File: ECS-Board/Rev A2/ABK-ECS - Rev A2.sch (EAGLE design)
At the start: 169 parts, among them J1 22-27-2061-06, J2 USB-B-S-RA, J3 1241050-5, J4 MSTBA2, J5 22-05-7068-06, J6 22-05-7028-02, J7 22-05-7068-06, J8 22-05-7028-02, K1 G6K-2G-Y, SW1 B3FS-1015, SW2 B3FS-1015, T1 EXMACHINA-LOGO-NAME, T10 MMBT2222AL, T11 IRLML5103TRPBF, T2 IRLML5103TRPBF, T3 MMBT2222AL, T4 MMBT2222AL, T5 IRLML5103TRPBF, T6 MMBT2222AL, T7 IRLML5103TRPBF, T8 MMBT2222AL, T9 IRLML5103TRPBF, U1 AT24C512C-SSHM-B, U2 LPC1768FBD100, U3 LT3686HDDPBF, U4 LT3686HDDPBF, U5 CD4050BD, X1 FC-135, X2 ASE-12, X3 3000

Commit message: Add rev A2 and modify board
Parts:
- added R75: 1K5, rcl:R-EU_R0603
- F1: value FUSE3557L -> 1812L110/24DR; device fuse2:FUSE3557L -> fuse2:1812L110/24DR
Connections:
- net MOTOR_CTR renamed R_VALIDATION
- removed net 230V-DETECTION: C20.1, R38.2, U2.P1[27]/CLKOUT/*USB_OVRCR/CAP0[1]
- net +3V3: now also R75.1, U2.VDDA
- net 230V_DETECTION: now also C20.1, R38.2
- net N$2: now also R75.2
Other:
- moved on the sheet: R4, R5

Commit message: Add input and output to the board and LDO 5V to 3.3V for FTDI connector
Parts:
- added C22, C23, C24: 0.1uF, rcl:C-EUC0603
- added C25, C26: 1u, rcl:C-EUC0603
- added D10, D11, D12, D13: 1N4148WS, diode:1N4148WS
- added J10: 22-05-7068-06, con-molex:22-05-7068-06
- added J9: 22-05-7028-02, con-molex:22-05-7028-02
- added LED17, LED18, LED19, LED20, LED21, LED22, LED23: Blue, led:LEDCHIPLED_0603
- added OK3, OK4: TLP283-4, optocoupler:TLP283-4
- added R100, R101, R102, R103: 1K5, rcl:R-EU_R0603
- added R104, R105, R106, R107, R76, R77, R78, R79: 4K7, rcl:R-EU_R0603
- added R108, R109, R110, R111, R80, R81, R82, R83: 1K, rcl:R-EU_R0603
- added R112, R113, R114, R115, R84, R85, R86, R87, R92, R93, R94, R95: 330, rcl:R-EU_R0603
- added R88, R89, R90, R91: 10K, rcl:R-EU_R0603
- added R96, R97, R98, R99: 100, rcl:R-EU_R0603
- added T12, T13, T14, T15: IRLML5103TRPBF, International_Rectifier_By_element14_Batch_1:IRLML5103TRPBF
- added T16, T17, T18, T19: MMBT2222AL, transistor:MMBT2222AL
- added U6, U7, U8: SN74LVC2G17DBVR, ti:SN74LVC2G17DBVR
- added U9: TC1264-3.3, microchip-6:TC1264-3.3
- J7: value 22-05-7068-06 -> 22-05-7058-05; device con-molex:22-05-7068-06 -> con-molex:22-05-7058-05; MPN 22-05-7068 -> (none); OC_NEWARK 89K0316 -> (none)
- J8: value 22-05-7028-02 -> 22-05-7068-06; device con-molex:22-05-7028-02 -> con-molex:22-05-7068-06; MPN 22-05-7028 -> 22-05-7068; OC_NEWARK 25M1728 -> 89K0316
- OK2: MF VISHAY/TELEFUNKEN -> (none); MPN TCMT4100 -> (none); OC_NEWARK 06H1639 -> (none)
- R10: value 10K -> 0R; MPN MCMR06X1002FTL -> MCMR06X000 PTL; OC_NEWARK 86T3506 -> 86T3500
- R11, R21: value 1K5 -> 10K; MPN MCMR06X1501FTL -> MCMR06X1002FTL; OC_NEWARK 86T3542 -> 86T3506
- R13: value 31K6 -> 1K5; MPN MCMR06X3162FTL -> MCMR06X1501FTL; OC_FARNELL 2073391 -> (none); OC_NEWARK 86T3613 -> 86T3542
- R15: value 4K7 -> 31K6; MPN MCMR06X4701FTL -> MCMR06X3162FTL; OC_FARNELL (none) -> 2073391; OC_NEWARK 86T3649 -> 86T3613
- R17: value 52K3 -> 4K7; MPN MC0063W0603152K3 -> MCMR06X4701FTL; OC_FARNELL 2073391 -> (none); OC_NEWARK 26M0962 -> 86T3649
- R18: value 10K -> 52K3; MPN MCMR06X1002FTL -> MC0063W0603152K3; OC_NEWARK 86T3506 -> 26M0962
- R19: value 31K6 -> 10K; MPN MCMR06X3162FTL -> MCMR06X1002FTL; OC_NEWARK 86T3613 -> 86T3506
- R20: value 10K -> 31K6; MPN MCMR06X1002FTL -> MCMR06X3162FTL; OC_NEWARK 86T3506 -> 86T3613
- R23: value 100 -> 1K5; MPN MCMR06X1000FTL -> MCMR06X1501FTL; OC_FARNELL (none) -> 2073391; OC_NEWARK 86T3504 -> 86T3542
- R24, R68, R69, R70: value 1K -> 100; MPN MCMR06X1001FTL -> MCMR06X1000FTL; OC_NEWARK 86T3505 -> 86T3504
- R32: value 4K7 -> 1K; MPN MCMR06X4701FTL -> MCMR06X1001FTL; OC_NEWARK 86T3649 -> 86T3505
- R37: value 1K5 -> 4K7; MPN MCMR06X1501FTL -> MCMR06X4701FTL; OC_NEWARK 86T3542 -> 86T3649
- R40, R41, R42, R43: value 1K5 -> 1K; MPN MCMR06X1501FTL -> MCMR06X1001FTL; OC_NEWARK 86T3542 -> 86T3505
- R44: value 330 -> 1K; MPN MCMR06X4701FTL -> MCMR06X1001FTL; OC_NEWARK 86T3649 -> 86T3505
- R45: value 10K -> 1K; MPN MCMR06X4701FTL -> MCMR06X1001FTL; OC_NEWARK 86T3649 -> 86T3505
- R46: value 100 -> 4K7; MPN MCMR06X1000FTL -> MCMR06X4701FTL; OC_NEWARK 86T3504 -> 86T3649
- R47: value 330 -> 4K7
- R48: value 10K -> 4K7
- R49, R51, R53: value 330 -> 1K5; MPN MCMR06X4701FTL -> MCMR06X1501FTL; OC_NEWARK 86T3649 -> 86T3542
- R50, R52, R54: value 10K -> 1K5; MPN MCMR06X4701FTL -> MCMR06X1501FTL; OC_NEWARK 86T3649 -> 86T3542
- R55, R56: value 100 -> 1K5; MPN MCMR06X1000FTL -> MCMR06X1501FTL; OC_NEWARK 86T3504 -> 86T3542
- R57: value 100 -> 10K; MPN MCMR06X1000FTL -> MCMR06X4701FTL; OC_NEWARK 86T3504 -> 86T3649
- R58: value 100 -> 330; MPN MCMR06X1000FTL -> MCMR06X4701FTL; OC_NEWARK 86T3504 -> 86T3649
- R59: value 1K5 -> 100; MPN MCMR06X1501FTL -> MCMR06X1000FTL; OC_NEWARK 86T3542 -> 86T3504
- R60, R61, R62: value 1K5 -> 10K; MPN MCMR06X1501FTL -> MCMR06X4701FTL; OC_NEWARK 86T3542 -> 86T3649
- R63: value 4K7 -> 10K
- R64, R65, R66: value 4K7 -> 330
- R67: value 1K -> 330; MPN MCMR06X1001FTL -> MCMR06X4701FTL; OC_NEWARK 86T3505 -> 86T3649
- R7: value 10K -> 1K5; MPN MCMR06X1002FTL -> MCMR06X1501FTL; OC_NEWARK 86T3506 -> 86T3542
- R71: value 330 -> 100; MPN MCMR06X3300FTL -> MCMR06X1000FTL; OC_NEWARK 86T3616 -> 86T3504
- R72, R73, R74: value 330 -> 1K5; MPN MCMR06X3300FTL -> MCMR06X1501FTL; OC_NEWARK 86T3616 -> 86T3542
- R8: value 0R -> 10K; MPN MCMR06X000 PTL -> MCMR06X1002FTL; OC_NEWARK 86T3500 -> 86T3506
- T11, T9: value IRLML5103TRPBF -> MMBT2222AL; device International_Rectifier_By_element14_Batch_1:IRLML5103TRPBF -> transistor:MMBT2222AL
- T4, T6: value MMBT2222AL -> IRLML5103TRPBF; device transistor:MMBT2222AL -> International_Rectifier_By_element14_Batch_1:IRLML5103TRPBF
- U5: value CD4050BD -> SN74LVC2G17DBVR; device TI-CD4050BD:CD4050BD -> ti:SN74LVC2G17DBVR
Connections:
- new net INPUT: LED15.A, R45.2, R48.1, U8.2A
- new net INPUT_MCU: U2.P0[16]/RXD1/SSEL0/SSEL, U8.2Y
- new net LED1: D10.1, J10-2.S, R88.2, T12.D
- new net LED1_MCU: R112.2, U2.P0[0]/RD1/TXD3/SDA1
- new net LED2: D11.1, J10-3.S, R89.2, T13.D
- new net LED2_MCU: R113.2, U2.P1[29]/MCOB2/PCAP1[1]/MAT0[1]
- new net LED3: D12.1, J10-4.S, R90.2, T14.D
- new net LED3_MCU: R114.2, U2.P1[28]/MCOA2/PCAP1[0]/MAT0[0]
- new net LED4: D13.1, J10-5.S, R91.2, T15.D
- new net LED4_MCU: R115.2, U2.P1[27]/CLKOUT/*USB_OVRCR/CAP0[1]
- new net N$100: OK2A.EMIT, R43.1
- new net N$101: OK2B.A, R41.2
- new net N$102: J7-3.S, R41.1
- new net N$103: OK2B.EMIT, R44.1
- new net N$104: OK2C.A, R42.2
- new net N$105: J7-2.S, R42.1
- new net N$106: OK2C.EMIT, R45.1
- new net N$107: LED13.C, R54.1
- new net N$108: LED14.C, R55.1
- new net N$109: LED15.C, R56.1
- new net N$31: LED20.A, R104.1, R108.1, R96.1
- new net N$33: OK4A.EMIT, R108.2
- new net N$34: LED21.A, R105.1, R109.1, R97.1
- new net N$35: OK4B.EMIT, R109.2
- new net N$36: LED22.A, R106.1, R110.1, R98.1
- new net N$37: LED23.A, R107.1, R111.1, R99.1
- new net N$38: OK4C.EMIT, R110.2
- new net N$39: OK4D.EMIT, R111.2
- new net N$40: OK4A.A, R112.1
- new net N$42: OK4B.A, R113.1
- new net N$43: OK4D.A, R115.1
- new net N$46: OK4C.A, R114.1
- new net N$66: LED20.C, R100.1
- new net N$67: LED21.C, R101.1
- new net N$68: LED22.C, R102.1
- new net N$69: LED23.C, R103.1
- new net N$71: R92.1, T12.G, T16.C
- new net N$72: R93.1, T13.G, T17.C
- new net N$77: R94.1, T14.G, T18.C
- new net N$78: R95.1, T15.G, T19.C
- new net N$81: OK2A.A, R40.2
- new net N$82: J7-4.S, R40.1
- new net N$84: R96.2, T16.B
- new net N$85: R97.2, T17.B
- new net N$98: R98.2, T18.B
- new net N$99: R99.2, T19.B
- new net SLOWFEED_1: LED13.A, R43.2, R46.1, U7.1A
- new net SLOWFEED_1_MCU: U2.P0[15]/TXD1/SCK0/SCK, U7.1Y
- new net SLOWFEED_2: LED14.A, R44.2, R47.1, U7.2A
- new net SLOWFEED_2_MCU: U2.P0[17]/CTS1/MISO0/MISO, U7.2Y
- net !RESET: now also R11.1; no longer R10.1
- net +24V: now also J10-1.S, J8-1.S, R17.2, R58.2, R64.2, R65.2, R66.2, R67.2, R92.2, R93.2, R94.2, R95.2, T12.S, T13.S, T14.S, T15.S, T4.S, T6.S; no longer R15.2, R44.2, R47.2, R49.2, R51.2, R53.2, T11.S, T9.S
- net +3V3: now also C22.1, C23.1, C24.1, C26.1, R11.2, R20.2, R23.2, R7.1, R8.2, U6.VCC, U7.VCC, U8.VCC, U9.VOUT; no longer R10.2, R19.2, R22.2, R7.2, R75.1
- net +5V: now also C25.1, J1-6.S, OK3A.COL, OK3B.COL, OK3C.COL, OK3D.COL, OK4A.COL, OK4B.COL, OK4C.COL, OK4D.COL, R18.2, R22.2, R37.1, U9.VIN; no longer OK2D.COL, R17.2, R21.2, R36.1
- net 230V_DETECTION: now also U8.1A; no longer U5.E
- net 230V_DETECTION_MCU: now also U8.1Y; no longer U5.K=E
- net BOOT_SELECT_P2_10: now also R9.1; no longer R8.1
- net BOOT_SELECT_P2_12: now also R10.1; no longer R9.1
- net BRAKE_CONTROL: now also D9.1, J8-5.S, R63.2, T7.D; no longer D8.1, J7-5.S, R54.2, T9.D
- net BRAKE_CONTROL_MCU: now also R87.2; no longer R74.2
- net CLUTCH_CONTROL: now also D8.1, J8-4.S, R62.2, T6.D; no longer D7.1, J7-4.S, R52.2, T7.D
- net CLUTCH_CONTROL_MCU: now also R86.2; no longer R73.2
- net DRIVE_STATUS_1: now also R31.2, R35.1, U6.1A; no longer R30.2, R34.1, U5.C
- net DRIVE_STATUS_1_MCU: now also U6.1Y; no longer U5.I=C
- net DRIVE_STATUS_2: now also R32.2, R36.1, U6.2A; no longer R31.2, R35.1, U5.D
- net DRIVE_STATUS_2_MCU: now also U6.2Y; no longer U5.J=D
- net EMERGENCY_STOP: now also R29.2, R33.1, U5.1A; no longer R28.2, R32.1, U5.A
- net EMERGENCY_STOP_MCU: now also U5.1Y; no longer U5.G=A
- net GND: now also C22.2, C23.2, C24.2, C25.2, C26.2, D10.2, D11.2, D12.2, D13.2, J10-6.S, J7-5.S, J8-6.S, J9-2.S, OK3A.C, OK3B.C, OK3C.C, OK3D.C, OK4A.C, OK4B.C, OK4C.C, OK4D.C, R100.2, R101.2, R102.2, R103.2, R104.2, R105.2, R106.2, R107.2, R13.2, R15.1, R19.1, R21.1, R36.2, R46.2, R47.2, R48.2, R49.2, R50.2, R51.2, R52.2, R53.2, R54.2, R55.2, R56.2, R57.1, R60.1, R61.1, R62.1, R63.1, R72.2, R73.2, R74.2, R75.2, R76.2, R77.2, R78.2, R79.2, R88.1, R89.1, R90.1, R91.1, T11.E, T16.E, T17.E, T18.E, T19.E, T9.E, U5.GND, U6.GND, U7.GND, U8.GND, U9.GND, U9.GND_2; no longer J7-6.S, J8-2.S, OK2D.C, R11.2, R13.1, R18.1, R20.1, R32.2, R37.2, R40.2, R41.2, R42.2, R43.2, R45.1, R48.1, R50.1, R52.1, R54.1, R59.2, R60.2, R61.2, R62.2, R63.2, R64.2, R65.2, R66.2, T4.E, T6.E, U5.VSS
- net LIMIT_SWITCH: now also R30.2, R34.1, U5.2A; no longer R29.2, R33.1, U5.B
- net LIMIT_SWITCH_MCU: now also U5.2Y; no longer U5.H=B
- net L_VALIDATION: now also D7.1, J8-3.S, R61.2; no longer D6.1, J7-3.S, R48.2
- net L_VALIDATION_MCU: now also R85.2; no longer R72.2
- net MOTOR_CONTROL_MCU: now also R59.2; no longer R46.2
- net N$1: now also R7.2; no longer R6.2
- net N$13: now also R20.1, R21.2; no longer R19.1, R20.2
- net N$17: now also R68.2, T8.B; no longer R55.2, T3.B
- net N$18: now also R64.1, T4.G, T8.C; no longer R51.1, T2.G, T3.C
- net N$19: now also R69.2, T9.B; no longer R56.2, T4.B
- net N$2: now also R6.2; no longer R75.2
- net N$20: now also R65.1, T9.C; no longer R47.1, T4.C
- net N$21: now also R70.2, T10.B; no longer R57.2, T6.B
- net N$22: now also R66.1, T10.C, T6.G; no longer R49.1, T6.C, T7.G
- net N$23: now also R71.2, T11.B; no longer R58.2, T8.B
- net N$24: now also R67.1, T11.C, T7.G; no longer R53.1, T8.C, T9.G
- net N$25: now also R59.1, T3.B; no longer R46.1, T10.B
- net N$26: now also R58.1, T2.G, T3.C; no longer R44.1, T10.C, T11.G
- net N$28: now also R24.2; no longer R23.2
- net N$29: now also R12.1; no longer R11.1
- net N$3: now also R13.1; no longer R12.1
- net N$30: now also D5.1, J9-1.S, R57.2, T2.D; no longer D9.1, J8-1.S, R45.2, T11.D
- net N$32: now also R24.1; no longer R23.1
- net N$4: now also R14.2; no longer R13.2
- net N$41: now also R25.2; no longer R24.2
- net N$44: now also R17.1; no longer R16.1
- net N$45: now also R16.1; no longer R15.1
- net N$47: now also R26.2; no longer R25.2
- net N$48: now also R27.2; no longer R26.2
- net N$49: now also R28.2; no longer R27.2
- net N$5: now also R10.2, R8.1; no longer R7.1, R8.2
- net N$50: now also R23.1; no longer R22.1
- net N$51: now also R22.1; no longer R21.1
- net N$52: now also R28.1; no longer R27.1
- net N$53: now also R27.1; no longer R26.1
- net N$54: now also R26.1; no longer R25.1
- net N$55: now also R25.1; no longer R24.1
- net N$56: now also R49.1; no longer R37.1
- net N$57: now also R50.1; no longer R40.1
- net N$58: now also R51.1; no longer R41.1
- net N$59: now also R52.1; no longer R42.1
- net N$61: now also R32.1; no longer R31.1
- net N$62: now also R31.1; no longer R30.1
- net N$63: now also R30.1; no longer R29.1
- net N$64: now also R29.1; no longer R28.1
- net N$65: now also R53.1; no longer R43.1
- net N$7: now also R15.2; no longer R14.2
- net N$73: now also R37.2; no longer R36.2
- net N$75: now also LED16.A, R68.1, R76.1, R80.1; no longer LED13.A, R55.1, R63.1, R67.1
- net N$76: now also OK3A.EMIT, R80.2; no longer OK2A.EMIT, R67.2
- net N$79: now also LED17.A, R69.1, R77.1, R81.1; no longer LED14.A, R56.1, R64.1, R68.1
- net N$80: now also OK3B.EMIT, R81.2; no longer OK2B.EMIT, R68.2
- net N$83: now also LED18.A, R70.1, R78.1, R82.1; no longer LED15.A, R57.1, R65.1, R69.1
- net N$86: now also LED19.A, R71.1, R79.1, R83.1; no longer LED16.A, R58.1, R66.1, R70.1
- net N$87: now also OK3C.EMIT, R82.2; no longer OK2C.EMIT, R69.2
- net N$88: now also OK3D.EMIT, R83.2; no longer OK2D.EMIT, R70.2
- net N$89: now also OK3A.A, R84.1; no longer OK2A.A, R71.1
- net N$9: now also R18.1, R19.2; no longer R17.1, R18.2
- net N$91: now also OK3B.A, R85.1; no longer OK2B.A, R72.1
- net N$92: now also OK3D.A, R87.1; no longer OK2D.A, R74.1
- net N$93: now also OK3C.A, R86.1; no longer OK2C.A, R73.1
- net N$94: now also LED16.C, R72.1; no longer LED13.C, R59.1
- net N$95: now also LED17.C, R73.1; no longer LED14.C, R60.1
- net N$96: now also LED18.C, R74.1; no longer LED15.C, R61.1
- net N$97: now also LED19.C, R75.1; no longer LED16.C, R62.1
- net R_VALIDATION: now also D6.1, J8-2.S, R60.2, T4.D; no longer D5.1, J7-2.S, R50.2, T2.D
- net R_VALIDATION_MCU: now also R84.2; no longer R71.2

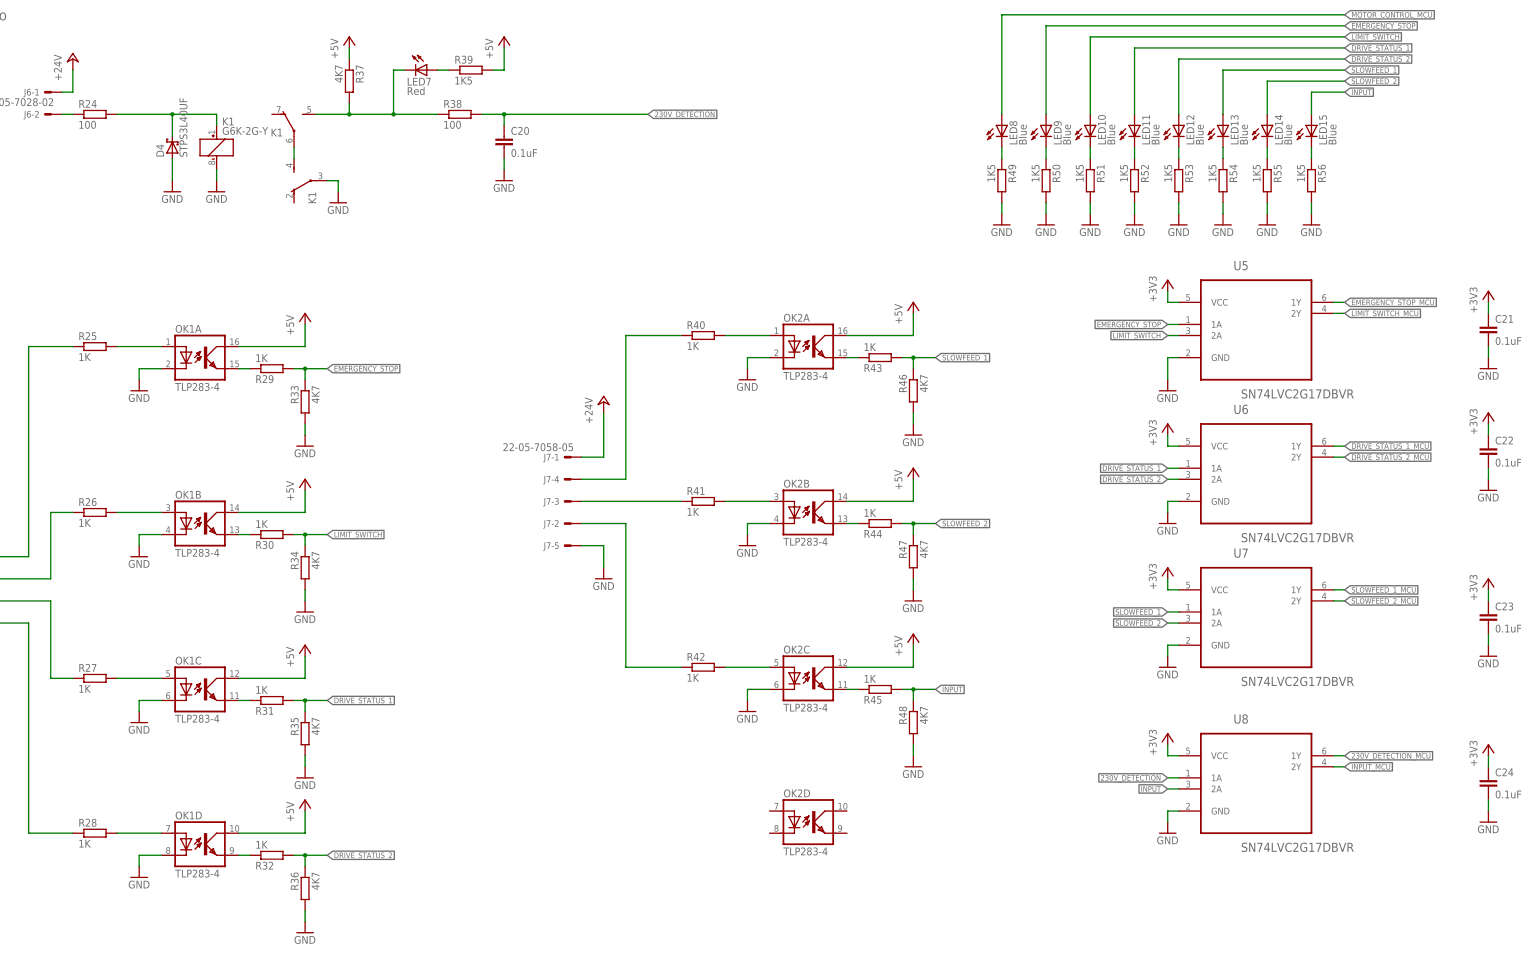
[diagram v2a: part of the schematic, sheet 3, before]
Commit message: Add pullup resistor on AT24C WP Separate +5V from ISP connector and the +5V general and add a diode Change +5V--->+3V3 conversion methode on input Wired OK2D
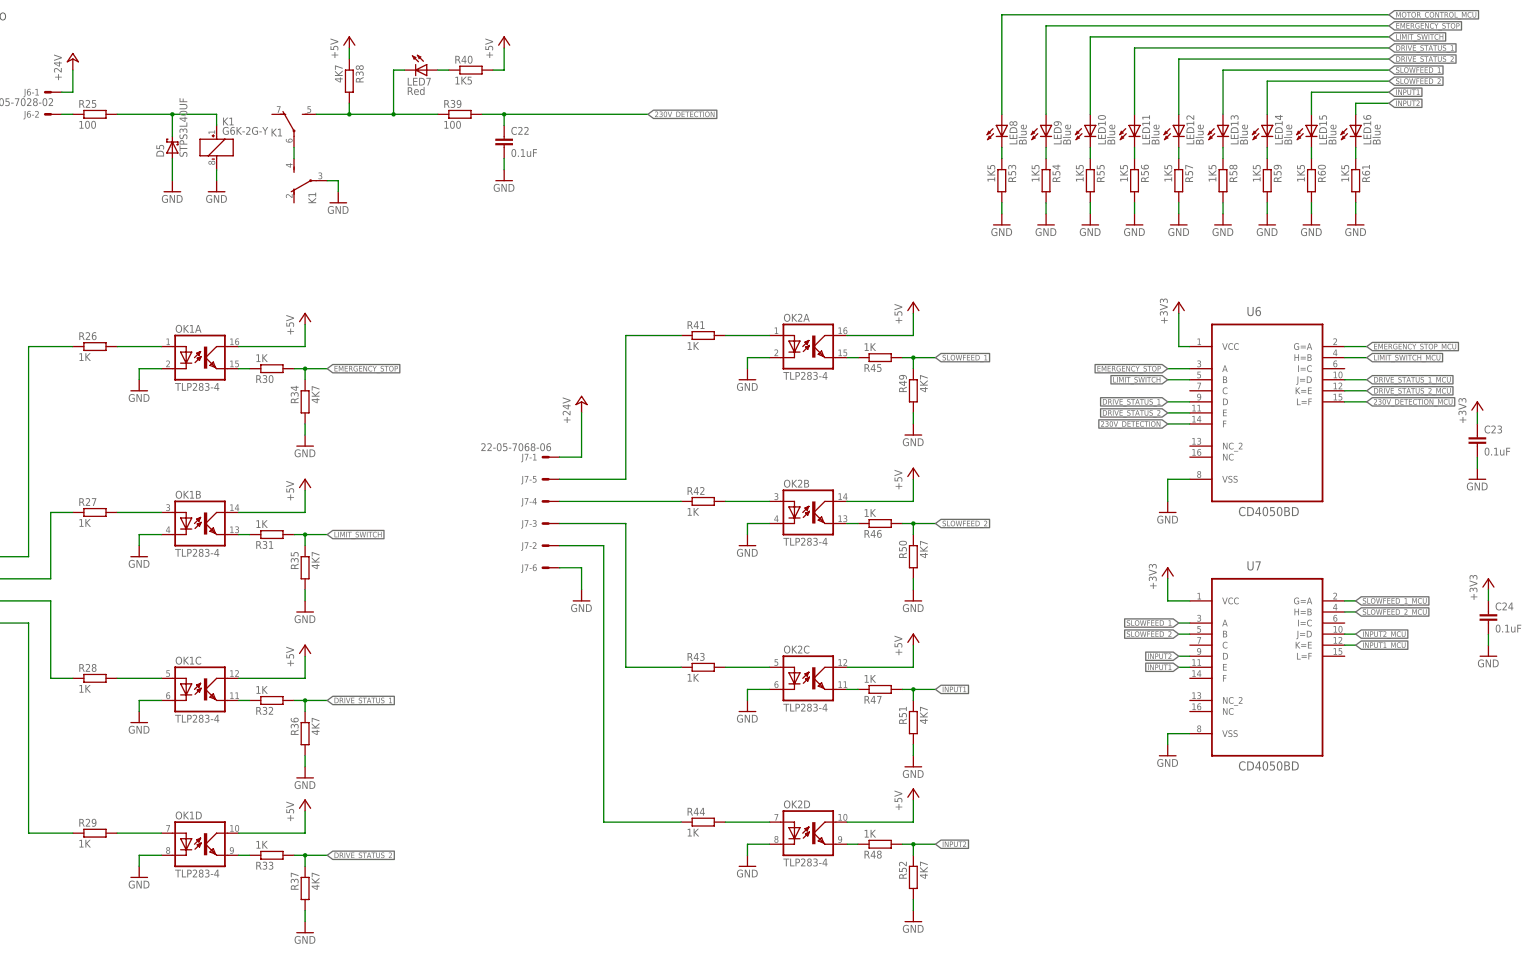
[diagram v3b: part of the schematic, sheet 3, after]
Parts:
- removed C25, C26: 1u, rcl:C-EUC0603
- removed U8: SN74LVC2G17DBVR, ti:SN74LVC2G17DBVR
- removed U9: TC1264-3.3, microchip-6:TC1264-3.3
- added D14: 1N4148WS, diode:1N4148WS
- added LED24: Blue, led:LEDCHIPLED_0603
- added R116: 1K, rcl:R-EU_R0603
- added R117, R118, R119, R120: 330, rcl:R-EU_R0603
- C20, C21: value 0.1uF -> 1u; MPN MC0603B104K160CT -> (none); OC_NEWARK 06R4923 -> (none)
- D5: value 1N4148WS -> STPS3L40UF; device diode:1N4148WS -> diode:STPS3L40UF; OC_NEWARK (none) -> 06X0873
- J7: value 22-05-7058-05 -> 22-05-7068-06; device con-molex:22-05-7058-05 -> con-molex:22-05-7068-06
- R100, R72: value 1K5 -> 330; MPN MCMR06X1501FTL -> MCMR06X4701FTL; OC_NEWARK 86T3542 -> 86T3649
- R101, R102, R103, R39, R73, R74, R75: value 1K5 -> 100; MPN MCMR06X1501FTL -> MCMR06X1000FTL; OC_NEWARK 86T3542 -> 86T3504
- R104, R76: value 4K7 -> 100; MPN MCMR06X4701FTL -> MCMR06X1000FTL; OC_NEWARK 86T3649 -> 86T3504
- R105, R106, R107, R77, R78, R79: value 4K7 -> 1K5; MPN MCMR06X4701FTL -> MCMR06X1501FTL; OC_NEWARK 86T3649 -> 86T3542
- R108, R40, R80: value 1K -> 1K5; MPN MCMR06X1001FTL -> MCMR06X1501FTL; OC_NEWARK 86T3505 -> 86T3542
- R109, R110, R111, R81, R82, R83: value 1K -> 4K7; MPN MCMR06X1001FTL -> MCMR06X4701FTL; OC_NEWARK 86T3505 -> 86T3649
- R11: value 10K -> 0R; MPN MCMR06X1002FTL -> MCMR06X000 PTL; OC_NEWARK 86T3506 -> 86T3500
- R112, R84: value 330 -> 4K7; MPN MCMR06X3300FTL -> MCMR06X4701FTL; OC_NEWARK 86T3616 -> 86T3649
- R113, R114, R115, R85, R86, R87: value 330 -> 1K; MPN MCMR06X3300FTL -> MCMR06X1001FTL; OC_NEWARK 86T3616 -> 86T3505
- R12, R22: value 1K5 -> 10K; MPN MCMR06X1501FTL -> MCMR06X1002FTL; OC_NEWARK 86T3542 -> 86T3506
- R14: value 31K6 -> 1K5; MPN MCMR06X3162FTL -> MCMR06X1501FTL; OC_FARNELL 2073391 -> (none); OC_NEWARK 86T3613 -> 86T3542
- R16: value 4K7 -> 31K6; MPN MCMR06X4701FTL -> MCMR06X3162FTL; OC_FARNELL (none) -> 2073391; OC_NEWARK 86T3649 -> 86T3613
- R18: value 52K3 -> 4K7; MPN MC0063W0603152K3 -> MCMR06X4701FTL; OC_FARNELL 2073391 -> (none); OC_NEWARK 26M0962 -> 86T3649
- R19: value 10K -> 52K3; MPN MCMR06X1002FTL -> MC0063W0603152K3; OC_NEWARK 86T3506 -> 26M0962
- R20: value 31K6 -> 10K; MPN MCMR06X3162FTL -> MCMR06X1002FTL; OC_NEWARK 86T3613 -> 86T3506
- R21: value 10K -> 31K6; MPN MCMR06X1002FTL -> MCMR06X3162FTL; OC_NEWARK 86T3506 -> 86T3613
- R24: value 100 -> 1K5; MPN MCMR06X1000FTL -> MCMR06X1501FTL; OC_FARNELL (none) -> 2073391; OC_NEWARK 86T3504 -> 86T3542
- R25: value 1K -> 100; MPN MCMR06X1001FTL -> MCMR06X1000FTL; OC_NEWARK 86T3505 -> 86T3504
- R33, R46, R47, R48: value 4K7 -> 1K; MPN MCMR06X4701FTL -> MCMR06X1001FTL; OC_NEWARK 86T3649 -> 86T3505
- R38: value 100 -> 4K7; MPN MCMR06X1000FTL -> MCMR06X4701FTL; OC_NEWARK 86T3504 -> 86T3649
- R4: value 33 -> 4K7; MPN MCMR06X33R0FTL -> MCMR06X4701FTL; OC_NEWARK 86T3614 -> 86T3649
- R49, R50, R51, R52: value 1K5 -> 4K7; MPN MCMR06X1501FTL -> MCMR06X4701FTL; OC_NEWARK 86T3542 -> 86T3649
- R57, R60, R61: value 10K -> 1K5; MPN MCMR06X4701FTL -> MCMR06X1501FTL; OC_NEWARK 86T3649 -> 86T3542
- R58: value 330 -> 1K5; MPN MCMR06X4701FTL -> MCMR06X1501FTL; OC_NEWARK 86T3649 -> 86T3542
- R59: value 100 -> 1K5; MPN MCMR06X1000FTL -> MCMR06X1501FTL; OC_NEWARK 86T3504 -> 86T3542
- R6: value 1K5 -> 33; MPN MCMR06X1501FTL -> MCMR06X33R0FTL; OC_NEWARK 86T3542 -> 86T3614
- R63: value 10K -> 330
- R64: value 330 -> 100; MPN MCMR06X4701FTL -> MCMR06X1000FTL; OC_NEWARK 86T3649 -> 86T3504
- R65, R66, R67, R93, R94, R95: value 330 -> 10K
- R68, R96: value 100 -> 10K; MPN MCMR06X1000FTL -> MCMR06X4701FTL; OC_NEWARK 86T3504 -> 86T3649
- R69, R70, R71, R97, R98, R99: value 100 -> 330; MPN MCMR06X1000FTL -> MCMR06X4701FTL; OC_NEWARK 86T3504 -> 86T3649
- R8: value 10K -> 1K5; MPN MCMR06X1002FTL -> MCMR06X1501FTL; OC_NEWARK 86T3506 -> 86T3542
- R88: value 10K -> 1K; MPN MCMR06X4701FTL -> MCMR06X1001FTL; OC_NEWARK 86T3649 -> 86T3505
- R89, R90, R91: value 10K -> 330; MPN MCMR06X4701FTL -> MCMR06X3300FTL; OC_NEWARK 86T3649 -> 86T3616
- R9: value 0R -> 10K; MPN MCMR06X000 PTL -> MCMR06X1002FTL; OC_NEWARK 86T3500 -> 86T3506
- R92: MPN MCMR06X4701FTL -> MCMR06X3300FTL; OC_NEWARK 86T3649 -> 86T3616
- U5: value SN74LVC2G17DBVR -> TC1264-3.3; device ti:SN74LVC2G17DBVR -> microchip-6:TC1264-3.3
- U6, U7: value SN74LVC2G17DBVR -> CD4050BD; device ti:SN74LVC2G17DBVR -> ti:CD4050BD
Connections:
- removed net INPUT: LED15.A, R45.2, R48.1, U8.2A
- removed net INPUT_MCU: U2.P0[16]/RXD1/SSEL0/SSEL, U8.2Y
- new net +5V/1: C20.1, D4.C, J1-6.S, U5.VIN
- new net INPUT1: LED15.A, R47.2, R51.1, U7.E
- new net INPUT1_MCU: U2.P0[16]/RXD1/SSEL0/SSEL, U7.K=E
- new net INPUT2: LED16.A, R48.2, R52.1, U7.D
- new net INPUT2_MCU: U2.P2[9]/USB_CONNECT/RXD2, U7.J=D
- new net N$110: OK2D.EMIT, R48.1
- new net N$111: OK2D.A, R44.2
- new net N$112: J7-2.S, R44.1
- new net N$90: LED16.C, R61.1
- net !RESET: now also R12.1; no longer R11.1
- net +24V: now also R100.2, R18.2, R63.2, R69.2, R70.2, R71.2, R72.2, R97.2, R98.2, R99.2; no longer R16.2, R58.2, R64.2, R65.2, R66.2, R67.2, R92.2, R93.2, R94.2, R95.2
- net +3V3: now also R1.1, R12.2, R21.2, R24.2, R4.2, R8.1, R9.2, U5.VOUT; no longer C22.1, C26.1, R11.2, R2.2, R20.2, R23.2, R6.1, R8.2, U5.VCC, U8.VCC, U9.VOUT
- net +5V: now also OK2D.COL, R19.2, R23.2, R38.1, R40.2; no longer C25.1, J1-6.S, R18.2, R22.2, R37.1, R39.2, U9.VIN
- net 230V_DETECTION: now also C22.1, R39.2, U6.F; no longer C20.1, R38.2, U8.1A
- net 230V_DETECTION_MCU: now also U6.L=F; no longer U8.1Y
- net BOOT_SELECT_P2_10: now also R10.1; no longer R9.1
- net BOOT_SELECT_P2_12: now also R11.1; no longer R10.1
- net BRAKE_CONTROL: now also D10.1, R68.2; no longer D9.1, R63.2
- net BRAKE_CONTROL_MCU: now also R92.2; no longer R87.2
- net CLUTCH_CONTROL: now also D9.1, R67.2; no longer D8.1, R62.2
- net CLUTCH_CONTROL_MCU: now also R91.2; no longer R86.2
- net DRIVE_STATUS_1: now also R32.2, R36.1, U6.D; no longer R31.2, R35.1, U6.1A
- net DRIVE_STATUS_1_MCU: now also U6.J=D; no longer U6.1Y
- net DRIVE_STATUS_2: now also R33.2, R37.1, U6.E; no longer R32.2, R36.1, U6.2A
- net DRIVE_STATUS_2_MCU: now also U6.K=E; no longer U6.2Y
- net EEPROM_SCL: now also R4.1; no longer R3.1
- net EEPROM_SDA: now also R3.1; no longer R2.1
- net EMERGENCY_STOP: now also R30.2, R34.1, U6.A; no longer R29.2, R33.1, U5.1A
- net EMERGENCY_STOP_MCU: now also U6.G=A; no longer U5.1Y
- net GND: now also D14.2, D5.A, J7-6.S, OK2D.C, R108.2, R109.2, R110.2, R111.2, R112.2, R14.2, R16.1, R2.2, R20.1, R22.1, R37.2, R57.2, R58.2, R59.2, R60.2, R61.2, R65.1, R66.1, R67.1, R68.1, R80.2, R81.2, R82.2, R83.2, R84.2, R93.1, R94.1, R95.1, R96.1, U5.GND_2, U6.VSS, U7.VSS; no longer C25.2, C26.2, D5.2, J7-5.S, R1.2, R100.2, R101.2, R102.2, R103.2, R104.2, R12.2, R14.1, R19.1, R21.1, R33.2, R46.2, R47.2, R48.2, R57.1, R60.1, R61.1, R63.1, R72.2, R73.2, R74.2, R75.2, R76.2, R88.1, R89.1, R90.1, R91.1, U6.GND, U7.GND, U8.GND, U9.GND, U9.GND_2
- net LED1: now also D11.1, R93.2; no longer D10.1, R88.2
- net LED1_MCU: now also R117.2; no longer R112.2
- net LED2: now also D12.1, R94.2; no longer D11.1, R89.2
- net LED2_MCU: now also R118.2; no longer R113.2
- net LED3: now also D13.1, R95.2; no longer D12.1, R90.2
- net LED3_MCU: now also R119.2; no longer R114.2
- net LED4: now also D14.1, R96.2; no longer D13.1, R91.2
- net LED4_MCU: now also R120.2; no longer R115.2
- net LIMIT_SWITCH: now also R31.2, R35.1, U6.B; no longer R30.2, R34.1, U5.2A
- net LIMIT_SWITCH_MCU: now also U6.H=B; no longer U5.2Y
- net L_VALIDATION: now also D8.1, R66.2; no longer D7.1, R61.2
- net L_VALIDATION_MCU: now also R90.2; no longer R85.2
- net MOTOR_CONTROL_MCU: now also R64.2; no longer R59.2
- net N$1: now also R6.1, R8.2; no longer R5.1, R7.2
- net N$100: now also R45.1; no longer R43.1
- net N$101: now also R42.2; no longer R41.2
- net N$102: now also J7-4.S, R42.1; no longer J7-3.S, R41.1
- net N$103: now also R46.1; no longer R44.1
- net N$104: now also R43.2; no longer R42.2
- net N$105: now also J7-3.S, R43.1; no longer J7-2.S, R42.1
- net N$106: now also R47.1; no longer R45.1
- net N$107: now also R58.1; no longer R54.1
- net N$108: now also R59.1; no longer R55.1
- net N$109: now also R60.1; no longer R56.1
- net N$13: now also R21.1, R22.2; no longer R20.1, R21.2
- net N$17: now also R73.2; no longer R68.2
- net N$18: now also R69.1; no longer R64.1
- net N$19: now also R74.2; no longer R69.2
- net N$2: now also R5.1, R7.2; no longer R4.1, R6.2
- net N$20: now also R70.1; no longer R65.1
- net N$21: now also R75.2; no longer R70.2
- net N$22: now also R71.1; no longer R66.1
- net N$23: now also R76.2; no longer R71.2
- net N$24: now also R72.1; no longer R67.1
- net N$25: now also R64.1; no longer R59.1
- net N$26: now also R63.1; no longer R58.1
- net N$27: now also R1.2, R2.1; no longer R1.1
- net N$28: now also D5.C, R25.2; no longer D4.C, R24.2
- net N$29: now also R13.1; no longer R12.1
- net N$3: now also R14.1; no longer R13.1
- net N$30: now also D6.1, R62.2; no longer D5.1, R57.2
- net N$31: now also LED21.A, R101.1, R109.1, R113.1; no longer LED20.A, R104.1, R108.1, R96.1
- net N$32: now also R25.1; no longer R24.1
- net N$33: now also R113.2; no longer R108.2
- net N$34: now also LED22.A, R102.1, R110.1, R114.1; no longer LED21.A, R105.1, R109.1, R97.1
- net N$35: now also R114.2; no longer R109.2
- net N$36: now also LED23.A, R103.1, R111.1, R115.1; no longer LED22.A, R106.1, R110.1, R98.1
- net N$37: now also LED24.A, R104.1, R112.1, R116.1; no longer LED23.A, R107.1, R111.1, R99.1
- net N$38: now also R115.2; no longer R110.2
- net N$39: now also R116.2; no longer R111.2
- net N$4: now also R15.2; no longer R14.2
- net N$40: now also R117.1; no longer R112.1
- net N$41: now also R26.2; no longer R25.2
- net N$42: now also R118.1; no longer R113.1
- net N$43: now also R120.1; no longer R115.1
- net N$44: now also R18.1; no longer R17.1
- net N$45: now also R17.1; no longer R16.1
- net N$46: now also R119.1; no longer R114.1
- net N$47: now also R27.2; no longer R26.2
- net N$48: now also R28.2; no longer R27.2
- net N$49: now also R29.2; no longer R28.2
- net N$5: now also R11.2, R9.1; no longer R8.1, R9.2
- net N$50: now also R24.1; no longer R23.1
- net N$51: now also R23.1; no longer R22.1
- net N$52: now also R29.1; no longer R28.1
- net N$53: now also R28.1; no longer R27.1
- net N$54: now also R27.1; no longer R26.1
- net N$55: now also R26.1; no longer R25.1
- net N$56: now also R53.1; no longer R49.1
- net N$57: now also R54.1; no longer R50.1
- net N$58: now also R55.1; no longer R51.1
- net N$59: now also R56.1; no longer R52.1
- net N$61: now also R33.1; no longer R32.1
- net N$62: now also R32.1; no longer R31.1
- net N$63: now also R31.1; no longer R30.1
- net N$64: now also R30.1; no longer R29.1
- net N$65: now also R57.1; no longer R53.1
- net N$66: now also LED21.C, R105.1; no longer LED20.C, R100.1
- net N$67: now also LED22.C, R106.1; no longer LED21.C, R101.1
- net N$68: now also LED23.C, R107.1; no longer LED22.C, R102.1
- net N$69: now also LED24.C, R108.1; no longer LED23.C, R103.1
- net N$7: now also R16.2; no longer R15.2
- net N$71: now also R97.1; no longer R92.1
- net N$72: now also R98.1; no longer R93.1
- net N$73: now also R38.2, R39.1; no longer R37.2, R38.1
- net N$74: now also R40.1; no longer R39.1
- net N$75: now also LED17.A, R73.1, R81.1, R85.1; no longer LED16.A, R68.1, R76.1, R80.1
- net N$76: now also R85.2; no longer R80.2
- net N$77: now also R99.1; no longer R94.1
- net N$78: now also R100.1; no longer R95.1
- net N$79: now also LED18.A, R74.1, R82.1, R86.1; no longer LED17.A, R69.1, R77.1, R81.1
- net N$80: now also R86.2; no longer R81.2
- net N$81: now also R41.2; no longer R40.2
- net N$82: now also J7-5.S, R41.1; no longer J7-4.S, R40.1
- net N$83: now also LED19.A, R75.1, R83.1, R87.1; no longer LED18.A, R70.1, R78.1, R82.1
- net N$84: now also R101.2; no longer R96.2
- net N$85: now also R102.2; no longer R97.2
- net N$86: now also LED20.A, R76.1, R84.1, R88.1; no longer LED19.A, R71.1, R79.1, R83.1
- net N$87: now also R87.2; no longer R82.2
- net N$88: now also R88.2; no longer R83.2
- net N$89: now also R89.1; no longer R84.1
- net N$9: now also R19.1, R20.2; no longer R18.1, R19.2
- net N$91: now also R90.1; no longer R85.1
- net N$92: now also R92.1; no longer R87.1
- net N$93: now also R91.1; no longer R86.1
- net N$94: now also LED17.C, R77.1; no longer LED16.C, R72.1
- net N$95: now also LED18.C, R78.1; no longer LED17.C, R73.1
- net N$96: now also LED19.C, R79.1; no longer LED18.C, R74.1
- net N$97: now also LED20.C, R80.1; no longer LED19.C, R75.1
- net N$98: now also R103.2; no longer R98.2
- net N$99: now also R104.2; no longer R99.2
- net R_VALIDATION: now also D7.1, R65.2; no longer D6.1, R60.2
- net R_VALIDATION_MCU: now also R89.2; no longer R84.2
- net SLOWFEED_1: now also R45.2, R49.1, U7.A; no longer R43.2, R46.1, U7.1A
- net SLOWFEED_1_MCU: now also U2.P0[17]/CTS1/MISO0/MISO, U7.G=A; no longer U2.P0[15]/TXD1/SCK0/SCK, U7.1Y
- net SLOWFEED_2: now also R46.2, R50.1, U7.B; no longer R44.2, R47.1, U7.2A
- net SLOWFEED_2_MCU: now also U2.P0[15]/TXD1/SCK0/SCK, U7.H=B; no longer U2.P0[17]/CTS1/MISO0/MISO, U7.2Y
- net USB_D_N: now also R5.2; no longer R4.2
- net USB_D_P: now also R6.2; no longer R5.2
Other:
- moved on the sheet: C22, C23, C24, D11, D12, D13, D6, D7, D8, D9, J7-1, J7-2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

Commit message: Final modifications before production version:
* Rename inputs and outputs to generic names
* Add silkscreen labels
* Move components for better layout in output block
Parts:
- added R121: 0R, rcl:R-EU_R0603
- LED21: value Blue -> 01.1
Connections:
- net 230V_DETECTION renamed INPUT3.1
- net 230V_DETECTION_MCU renamed INPUT3.1_MCU
- net BRAKE_CONTROL renamed OUTPUT2.4
- net BRAKE_CONTROL_MCU renamed OUTPUT2.4_MCU
- net CLUTCH_CONTROL renamed OUTPUT2.3
- net CLUTCH_CONTROL_MCU renamed OUTPUT2.3_MCU
- net DRIVE_STATUS_1 renamed INPUT2.2
- net DRIVE_STATUS_1_MCU renamed INPUT2.2_MCU
- net DRIVE_STATUS_2 renamed INPUT2.1
- net DRIVE_STATUS_2_MCU renamed INPUT2.1_MCU
- net EMERGENCY_STOP renamed INPUT2.4
- net EMERGENCY_STOP_MCU renamed INPUT2.4_MCU
- net INPUT1 renamed INPUT1.2
- net INPUT1_MCU renamed INPUT1.2_MCU
- net INPUT2 renamed INPUT1.1
- net INPUT2_MCU renamed INPUT1.1_MCU
- net LED1 renamed OUTPUT1.1
- net LED1_MCU renamed OUTPUT1.1_MCU
- net LED2 renamed OUTPUT1.2
- net LED2_MCU renamed OUTPUT1.2_MCU
- net LED3 renamed OUTPUT1.3
- net LED3_MCU renamed OUTPUT1.3_MCU
- net LED4 renamed OUTPUT1.4
- net LED4_MCU renamed OUTPUT1.4_MCU
- net LED_DEBUG renamed ONBOARD_LED2
- net LIMIT_SWITCH renamed INPUT2.3
- net LIMIT_SWITCH_MCU renamed INPUT2.3_MCU
- net L_VALIDATION renamed OUTPUT2.2
- net L_VALIDATION_MCU renamed OUTPUT2.2_MCU
- net MOTOR_CONTROL_MCU renamed OUTPUT3.2_MCU
- net N$30 renamed MOTOR_VFQ
- net R_VALIDATION renamed OUTPUT2.1
- net R_VALIDATION_MCU renamed OUTPUT2.1_MCU
- net SLOWFEED_1 renamed INPUT1.4
- net SLOWFEED_1_MCU renamed INPUT1.4_MCU
- net SLOWFEED_2 renamed INPUT1.3
- net SLOWFEED_2_MCU renamed INPUT1.3_MCU
- net USB_UP_LED renamed ONBOARD_LED1
- new net ISP_RTS: J1-6.S, R121.2
- net +5V/1: now also J1-3.S; no longer J1-6.S
- net BOOT_SELECT_P2_10: now also R121.1
